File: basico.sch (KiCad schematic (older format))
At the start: 14 parts, among them P1 Power, P10 CONN_01X01, P11 CONN_01X01, P12 CONN_01X01, P13 CONN_01X01, P2 Analog, P3 Analog, P4 Digital, P5 PWM, P6 PWM, P7 Communication, P8 CONN_01X01, P9 CONN_01X01

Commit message: Empezamos a mapear cada pin
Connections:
- wire segments 172 -> 175
- no-connect marks 55 -> 83
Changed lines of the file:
@@
 Wire Wire Line
 	6950 3550 7150 3550
-NoConn ~ 3000 1750
-NoConn ~ 3000 1850
-NoConn ~ 3000 1950
 NoConn ~ 3000 2050
 NoConn ~ 3000 2150
@@
 Text Label 8900 2450 0    60   ~ 0
 A0
+NoConn ~ 8600 1550
+NoConn ~ 8900 1200
+NoConn ~ 10400 2450
+NoConn ~ 10500 4650
+NoConn ~ 8900 3800
+NoConn ~ 8900 4000
+NoConn ~ 8900 4100
+NoConn ~ 9300 5650
+NoConn ~ 9400 5650
+NoConn ~ 9500 5650
+NoConn ~ 9600 5650
+NoConn ~ 9700 5650
+NoConn ~ 9800 5650
+NoConn ~ 9900 5650
+NoConn ~ 10000 5650
+NoConn ~ 10000 4650
+NoConn ~ 10100 5650
+NoConn ~ 10300 4650
+NoConn ~ 10300 5650
+NoConn ~ 10400 5650
+NoConn ~ 10500 5650
+NoConn ~ 10400 3900
+NoConn ~ 10400 3500
+NoConn ~ 10400 1550
+NoConn ~ 10400 1650
+NoConn ~ 10400 1750
+NoConn ~ 10400 2750
+NoConn ~ 10400 2650
+NoConn ~ 10400 2550
+NoConn ~ 10400 2950
+NoConn ~ 10400 1350
+Text Label 3650 1750 0    50   ~ 0
+A0
+Wire Wire Line
+	3000 1750 3650 1750
+Wire Wire Line
+	3000 1850 3650 1850
+Text Label 3650 1850 0    50   ~ 0
+A1
+Wire Wire Line
+	3000 1950 3650 1950
+Text Label 3650 1950 0    50   ~ 0
+A2
 $EndSCHEMATC

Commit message: Mas actualizaciones de esquematico
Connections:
- net labels added: Ar_0, Ar_1, Ar_10, Ar_11, Ar_12, Ar_13, Ar_14, Ar_15, Ar_16, Ar_17, Ar_18, Ar_19, Ar_2, Ar_20, Ar_21, Ar_22, Ar_23, Ar_24, Ar_25, Ar_26, Ar_27, Ar_28, Ar_29, Ar_3, Ar_30, Ar_31, Ar_32, Ar_33, Ar_34, Ar_35, Ar_36, Ar_37, Ar_38, Ar_39, Ar_4, Ar_40, Ar_41, Ar_42, Ar_43, Ar_44, Ar_45, Ar_46, Ar_47, Ar_48, Ar_49, Ar_5, Ar_50, Ar_51, Ar_52, Ar_53, Ar_6, Ar_7, Ar_8, Ar_9, Ar_A0, Ar_A1, Ar_A10, Ar_A11, Ar_A12, Ar_A13, Ar_A14, Ar_A15, Ar_A2, Ar_A3, Ar_A4, Ar_A5, Ar_A6, Ar_A7, Ar_A8, Ar_A9, Ar_AREF, Ar_IOREF, Ar_Reset, Ar_SCL, Ar_SDA, Ar_Vin
- net labels removed: 0(Rx0), 1(Tx0), 10(**), 11(**), 12(**), 13(**), 14(Tx3), 15(Rx3), 16(Tx2), 17(Rx2), 18(Tx1), 19(Rx1), 2(**), 20(SDA), 21(SCL), 22, 23, 24, 25, 26, 27, 28, 29, 3(**), 30, 31, 32, 33, 34, 35, 36, 37, 38, 39, 4(**), 40, 41, 42, 43, 44, 45, 46, 47, 48, 49, 5(**), 50(MISO), 51(MOSI), 52(SCK), 53(SS), 6(**), 7(**), 8(**), 9(**), A0, A1, A10, A11, A12, A13, A14, A15, A2, A3, A4, A5, A6, A7, A8, A9, AREF, IOREF, Reset, SCL, SDA, Vin
- wire segments 175 -> 206
- no-connect marks 83 -> 52

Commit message: completado el esquematico
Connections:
- wire segments 206 -> 214
- no-connect marks 52 -> 44
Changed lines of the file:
@@
 L basico-rescue:GNDA #PWR017
 U 1 1 57A7AE5D
-P 5500 2000
-F 0 "#PWR017" H 5500 1750 50  0001 C CNN
-F 1 "GNDA" H 5500 1850 50  0000 C CNN
-F 2 "" H 5500 2000 50  0000 C CNN
-F 3 "" H 5500 2000 50  0000 C CNN
-	1    5500 2000
-	1    0    0    -1
-$EndComp
-Wire Wire Line
-	5750 1950 5500 1950
-Wire Wire Line
-	5500 1950 5500 2000
+P 5100 2000
+F 0 "#PWR017" H 5100 1750 50  0001 C CNN
+F 1 "GNDA" H 5100 1850 50  0000 C CNN
+F 2 "" H 5100 2000 50  0000 C CNN
+F 3 "" H 5100 2000 50  0000 C CNN
+	1    5100 2000
+	1    0    0    -1
+$EndComp
+Wire Wire Line
+	5750 1950 5100 1950
+Wire Wire Line
+	5100 1950 5100 2000
 Wire Wire Line
 	6950 1950 7000 1950
@@
 Wire Wire Line
 	6950 3550 7150 3550
-NoConn ~ 3000 2050
-NoConn ~ 3000 2150
-NoConn ~ 3000 2250
-NoConn ~ 3000 2350
-NoConn ~ 1800 2050
 NoConn ~ 1800 2350
 NoConn ~ 5750 1750
 NoConn ~ 5750 1850
-NoConn ~ 5750 2050
-NoConn ~ 5750 2150
-NoConn ~ 5750 2250
 NoConn ~ 5750 2350
 NoConn ~ 5750 2450
@@
 Wire Wire Line
 	3000 2650 3650 2650
+Text Label 3650 2850 0    50   ~ 0
+Ar_A3
+Text Label 1300 3250 0    50   ~ 0
+Ar_A4
+Text Label 3650 3050 0    50   ~ 0
+Ar_A5
+Wire Wire Line
+	1800 2050 1250 2050
+Text Label 1250 2050 0    50   ~ 0
+Ar_A6
+Wire Wire Line
+	3000 2050 3650 2050
+Text Label 3650 2050 0    50   ~ 0
+Ar_A7
+Wire Wire Line
+	3000 2150 3650 2150
+Text Label 3650 2150 0    50   ~ 0
+Ar_A8
+Wire Wire Line
+	5750 2050 5400 2050
+Wire Wire Line
+	5750 2150 5400 2150
+Wire Wire Line
+	5750 2250 5400 2250
+Text Label 3650 2650 0    50   ~ 0
+Ar_A13
+Text Label 5400 2250 0    50   ~ 0
+Ar_9
+Text Label 5400 2150 0    50   ~ 0
+Ar_10
+Text Label 5400 2050 0    50   ~ 0
+Ar_11
+Wire Wire Line
+	3000 2250 3650 2250
+Wire Wire Line
+	3000 2350 3650 2350
+Text Label 3650 2250 0    50   ~ 0
+Ar_11
+Text Label 3650 2350 0    50   ~ 0
+Ar_4
 $EndSCHEMATC

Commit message: Remove unused components. Update PCB
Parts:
- removed P10, P11, P12, P13, P8, P9: CONN_01X01, footprint:Arduino_1pin, symbol Connector_Generic:Conn_01x01
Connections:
- no-connect marks 44 -> 38
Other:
- note removed: "Holes"
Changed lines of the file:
@@
 Text Notes 8375 575  0    60   ~ 0
 Shield for Arduino Mega Rev 3
-Text Notes 10700 1000 0    60   ~ 0
-Holes
-$Comp
-L Connector_Generic:Conn_01x01 P8
-U 1 1 56D70B71
-P 10600 650
-F 0 "P8" V 10700 650 31  0000 C CNN
-F 1 "CONN_01X01" V 10700 650 50  0001 C CNN
-F 2 "footprint:Arduino_1pin" H 10600 650 50  0001 C CNN
-F 3 "" H 10600 650 50  0000 C CNN
-	1    10600 650
-	0    -1   -1   0
-$EndComp
-$Comp
-L Connector_Generic:Conn_01x01 P9
-U 1 1 56D70C9B
-P 10700 650
-F 0 "P9" V 10800 650 31  0000 C CNN
-F 1 "CONN_01X01" V 10800 650 50  0001 C CNN
-F 2 "footprint:Arduino_1pin" H 10700 650 50  0001 C CNN
-F 3 "" H 10700 650 50  0000 C CNN
-	1    10700 650
-	0    -1   -1   0
-$EndComp
-$Comp
-L Connector_Generic:Conn_01x01 P10
-U 1 1 56D70CE6
-P 10800 650
-F 0 "P10" V 10900 650 31  0000 C CNN
-F 1 "CONN_01X01" V 10900 650 50  0001 C CNN
-F 2 "footprint:Arduino_1pin" H 10800 650 50  0001 C CNN
-F 3 "" H 10800 650 50  0000 C CNN
-	1    10800 650
-	0    -1   -1   0
-$EndComp
-$Comp
-L Connector_Generic:Conn_01x01 P11
-U 1 1 56D70D2C
-P 10900 650
-F 0 "P11" V 11000 650 31  0000 C CNN
-F 1 "CONN_01X01" V 11000 650 50  0001 C CNN
-F 2 "footprint:Arduino_1pin" H 10900 650 50  0001 C CNN
-F 3 "" H 10900 650 50  0000 C CNN
-	1    10900 650
-	0    -1   -1   0
-$EndComp
-$Comp
-L Connector_Generic:Conn_01x01 P12
-U 1 1 56D711A2
-P 11000 650
-F 0 "P12" V 11100 650 31  0000 C CNN
-F 1 "CONN_01X01" V 11100 650 50  0001 C CNN
-F 2 "footprint:Arduino_1pin" H 11000 650 50  0001 C CNN
-F 3 "" H 11000 650 50  0000 C CNN
-	1    11000 650
-	0    -1   -1   0
-$EndComp
-$Comp
-L Connector_Generic:Conn_01x01 P13
-U 1 1 56D711F0
-P 11100 650
-F 0 "P13" V 11200 650 31  0000 C CNN
-F 1 "CONN_01X01" V 11200 650 50  0001 C CNN
-F 2 "footprint:Arduino_1pin" H 11100 650 50  0001 C CNN
-F 3 "" H 11100 650 50  0000 C CNN
-	1    11100 650
-	0    -1   -1   0
-$EndComp
-NoConn ~ 10600 850
-NoConn ~ 10700 850
-NoConn ~ 10800 850
-NoConn ~ 10900 850
-NoConn ~ 11000 850
-NoConn ~ 11100 850
 Text Notes 9650 1350 0    60   ~ 0
 1
@@
 	9350 1450 9250 1450
 Wire Notes Line
-	10450 1000 10450 500
-Wire Notes Line
-	11200 1000 10450 1000
-Wire Notes Line
 	9850 650  9850 475

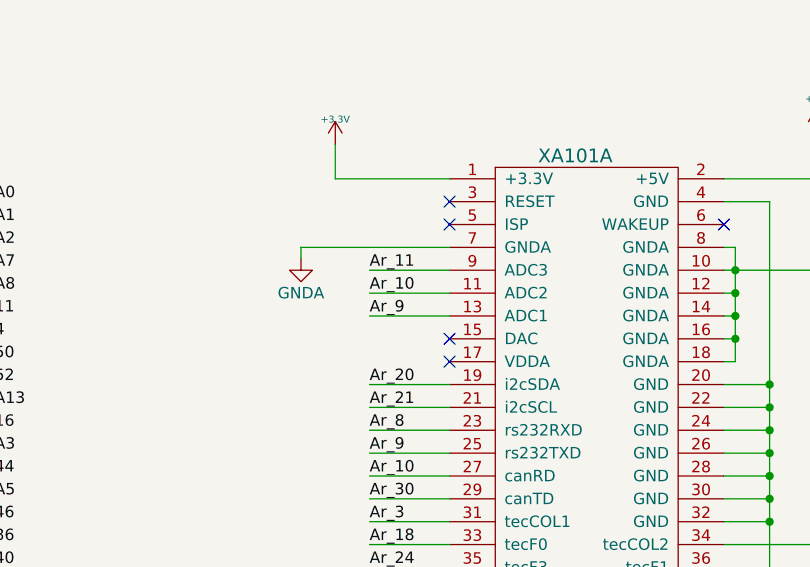
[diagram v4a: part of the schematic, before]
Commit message: Fix wrong mapping for analog channels
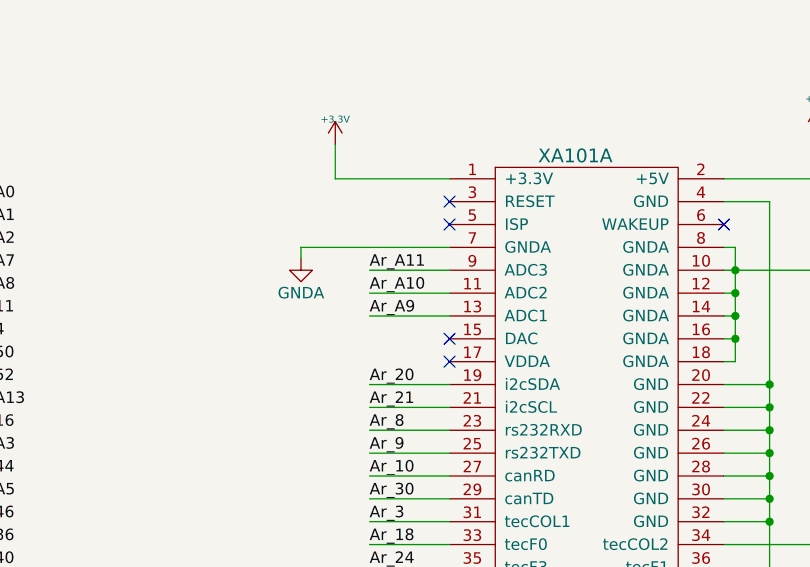
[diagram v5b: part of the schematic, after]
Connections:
- net Ar_10: no longer XA101.11 (ADC2)
- net Ar_11: no longer XA101.9 (ADC3)
- net Ar_9: no longer XA101.13 (ADC1)
- net Ar_A10: now also XA101.11 (ADC2)
- net Ar_A11: now also XA101.9 (ADC3)
- net Ar_A9: now also XA101.13 (ADC1)
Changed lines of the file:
@@
 Ar_A13
 Text Label 5400 2250 0    50   ~ 0
-Ar_9
+Ar_A9
 Text Label 5400 2150 0    50   ~ 0
-Ar_10
+Ar_A10
 Text Label 5400 2050 0    50   ~ 0
-Ar_11
+Ar_A11
 Wire Wire Line
 	3000 2250 3650 2250

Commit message: All routes done
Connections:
- net +3.3VP: no longer XA101.1 (+3.3V)
- net +5V: no longer P4.35 (Pin_35), P4.36 (Pin_36), XA101.2 (+5V)
- net GND: no longer P4.1 (Pin_1), P4.2 (Pin_2), XA101.20 (GND), XA101.22 (GND), XA101.24 (GND), XA101.26 (GND), XA101.28 (GND), XA101.30 (GND), XA101.32 (GND), XA101.38 (GND), XA101.4 (GND), XA101.40 (GND), XA101.51 (GND), XA101.53 (GND), XA101.57 (GND), XA101.59 (GND), XA101.65 (GND), XA101.67 (GND), XA101.77 (GND), XA101.79 (GND)
- no-connect marks 38 -> 62
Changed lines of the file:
@@
-$EndComp
-$Comp
-L basico-rescue:+3.3V #PWR01
-U 1 1 560EB699
-P 5250 1500
-F 0 "#PWR01" H 5250 1460 30  0001 C CNN
-F 1 "+3.3V" H 5250 1610 30  0000 C CNN
-F 2 "" H 5250 1500 60  0000 C CNN
-F 3 "" H 5250 1500 60  0000 C CNN
-	1    5250 1500
-	1    0    0    -1
-$EndComp
-$Comp
-L basico-rescue:+5V #PWR02
-U 1 1 560EB7BE
-P 7350 1450
-F 0 "#PWR02" H 7350 1540 20  0001 C CNN
-F 1 "+5V" H 7350 1600 30  0000 C CNN
-F 2 "" H 7350 1450 60  0000 C CNN
-F 3 "" H 7350 1450 60  0000 C CNN
-	1    7350 1450
-	1    0    0    -1
 $EndComp
 $Comp
 L basico-rescue:PWR_FLAG #FLG04
 U 1 1 560EDE73
-P 1300 3600
-F 0 "#FLG04" H 1300 3695 30  0001 C CNN
-F 1 "PWR_FLAG" H 1300 3780 30  0000 C CNN
-F 2 "" H 1300 3600 60  0000 C CNN
-F 3 "" H 1300 3600 60  0000 C CNN
-	1    1300 3600
+P 700 1900
+F 0 "#FLG04" H 700 1995 30  0001 C CNN
+F 1 "PWR_FLAG" H 700 2080 30  0000 C CNN
+F 2 "" H 700 1900 60  0000 C CNN
+F 3 "" H 700 1900 60  0000 C CNN
+	1    700  1900
 	-1   0    0    1
 $EndComp
@@
 	1    0    0    -1
 $EndComp
-$Comp
-L basico-rescue:GND #PWR06
-U 1 1 57A7A207
-P 7150 3750
-F 0 "#PWR06" H 7150 3750 30  0001 C CNN
-F 1 "GND" H 7150 3680 30  0001 C CNN
-F 2 "" H 7150 3750 60  0000 C CNN
-F 3 "" H 7150 3750 60  0000 C CNN
-	1    7150 3750
-	1    0    0    -1
-$EndComp
-Wire Wire Line
-	7150 1750 7150 2550
-Wire Wire Line
-	7150 3450 6950 3450
-Connection ~ 7150 3550
-Wire Wire Line
-	7150 3150 6950 3150
-Connection ~ 7150 3450
-Wire Wire Line
-	7150 3050 6950 3050
-Connection ~ 7150 3150
-Wire Wire Line
-	7150 2950 6950 2950
-Connection ~ 7150 3050
-Wire Wire Line
-	7150 2850 6950 2850
-Connection ~ 7150 2950
-Wire Wire Line
-	7150 2550 6950 2550
-Connection ~ 7150 2850
-Wire Wire Line
-	6950 2650 7150 2650
-Connection ~ 7150 2650
-Wire Wire Line
-	6950 2750 7150 2750
-Connection ~ 7150 2750
-Wire Wire Line
-	6950 1750 7150 1750
-Connection ~ 7150 2550
 Wire Wire Line
 	1600 1750 1600 1850
 Wire Wire Line
-	1600 3450 1800 3450
-Connection ~ 1600 3550
-Wire Wire Line
-	1600 2950 1800 2950
-Connection ~ 1600 3450
-Wire Wire Line
-	1600 2850 1800 2850
-Connection ~ 1600 2950
-Wire Wire Line
-	1600 2550 1800 2550
-Connection ~ 1600 2850
-Wire Wire Line
-	1600 2450 1800 2450
-Connection ~ 1600 2550
-Wire Wire Line
-	1600 2250 1800 2250
-Connection ~ 1600 2450
-Wire Wire Line
-	1600 2150 1800 2150
-Connection ~ 1600 2250
-Wire Wire Line
 	1600 1950 1800 1950
-Connection ~ 1600 2150
 Wire Wire Line
 	1600 1850 1800 1850
-Connection ~ 1600 1950
 Wire Wire Line
 	1600 1750 1800 1750
@@
 L basico-rescue:GNDD #PWR012
 U 1 1 57A7AB5F
-P 1600 3700
-F 0 "#PWR012" H 1600 3450 50  0001 C CNN
-F 1 "GNDD" H 1600 3550 50  0000 C CNN
-F 2 "" H 1600 3700 50  0000 C CNN
-F 3 "" H 1600 3700 50  0000 C CNN
-	1    1600 3700
+P 1000 2000
+F 0 "#PWR012" H 1000 1750 50  0001 C CNN
+F 1 "GNDD" H 1000 1850 50  0000 C CNN
+F 2 "" H 1000 2000 50  0000 C CNN
+F 3 "" H 1000 2000 50  0000 C CNN
+	1    1000 2000
 	1    0    0    -1
 $EndComp
@@
 	1    0    0    -1
 $EndComp
-$Comp
-L basico-rescue:GNDA #PWR017
-U 1 1 57A7AE5D
-P 5100 2000
-F 0 "#PWR017" H 5100 1750 50  0001 C CNN
-F 1 "GNDA" H 5100 1850 50  0000 C CNN
-F 2 "" H 5100 2000 50  0000 C CNN
-F 3 "" H 5100 2000 50  0000 C CNN
-	1    5100 2000
-	1    0    0    -1
-$EndComp
-Wire Wire Line
-	5750 1950 5100 1950
-Wire Wire Line
-	5100 1950 5100 2000
 Wire Wire Line
 	6950 1950 7000 1950
@@
 Wire Wire Line
 	3450 1650 3450 1400
-Wire Wire Line
-	5250 1650 5250 1500
-Wire Wire Line
-	6950 1650 7350 1650
-Wire Wire Line
-	7350 1650 7350 1450
-Wire Wire Line
-	5250 1650 5750 1650
-Wire Wire Line
-	6950 3550 7150 3550
 NoConn ~ 1800 2350
 NoConn ~ 5750 1750
@@
 NoConn ~ 6950 1850
 Wire Wire Line
-	7150 3550 7150 3750
-Wire Wire Line
-	7150 3450 7150 3550
-Wire Wire Line
-	7150 3150 7150 3450
-Wire Wire Line
-	7150 3050 7150 3150
-Wire Wire Line
-	7150 2950 7150 3050
-Wire Wire Line
-	7150 2850 7150 2950
-Wire Wire Line
-	7150 2650 7150 2750
-Wire Wire Line
-	7150 2750 7150 2850
-Wire Wire Line
-	7150 2550 7150 2650
-Wire Wire Line
-	1600 3550 1600 3700
-Wire Wire Line
-	1600 3550 1800 3550
-Wire Wire Line
-	1600 3450 1600 3550
-Wire Wire Line
-	1600 2950 1600 3450
-Wire Wire Line
-	1600 2850 1600 2950
-Wire Wire Line
-	1600 2550 1600 2850
-Wire Wire Line
-	1600 2450 1600 2550
-Wire Wire Line
-	1600 2250 1600 2450
-Wire Wire Line
-	1600 2150 1600 2250
-Wire Wire Line
-	1600 1950 1600 2150
+	1000 1850 1000 2000
+Wire Wire Line
+	1000 1850 1600 1850
 Wire Wire Line
 	1600 1850 1600 1950
@@
 Wire Wire Line
 	10250 1450 10150 1450
-$Comp
-L power:GND #PWR0103
-U 1 1 56D758F6
-P 8650 5750
-F 0 "#PWR0103" H 8650 5500 50  0001 C CNN
-F 1 "GND" H 8650 5600 50  0000 C CNN
-F 2 "" H 8650 5750 50  0000 C CNN
-F 3 "" H 8650 5750 50  0000 C CNN
-	1    8650 5750
-	1    0    0    -1
-$EndComp
 Wire Notes Line
 	11200 6050 8350 6050
@@
 Text Notes 7850 -250 0    79   Italic 16
 Este diseño puede copiarse para iniciar un poncho simple. \n1) Copiar toda la carpeta "Basico" , renombrando \n   la misma al nombre del poncho.\n2) Renombrar los archivos "basico.xxx" manteniendo \n    las extensiones pero cambiando a un nombre \n    descriptivo del poncho. Evitar acentos, espacios y \n    caracteres ascii esxtendidos.
-Wire Wire Line
-	8650 5350 8650 5750
-Wire Wire Line
-	8650 4850 8650 5350
-Wire Wire Line
-	10750 4850 10750 5350
-Wire Wire Line
-	10750 4550 10750 4850
-Connection ~ 10750 4850
-$Comp
-L power:+5V #PWR0104
-U 1 1 56D75AB8
-P 10750 4550
-F 0 "#PWR0104" H 10750 4400 50  0001 C CNN
-F 1 "+5V" H 10750 4690 50  0000 C CNN
-F 2 "" H 10750 4550 50  0000 C CNN
-F 3 "" H 10750 4550 50  0000 C CNN
-	1    10750 4550
-	1    0    0    -1
-$EndComp
-Wire Wire Line
-	10750 4850 10600 4850
-Wire Wire Line
-	10750 5350 10600 5350
-Connection ~ 8650 5350
-Wire Wire Line
-	8900 5350 8650 5350
-Wire Wire Line
-	8900 4850 8650 4850
 Wire Wire Line
 	9000 5350 9000 5750
@@
 	1800 3250 1300 3250
 Wire Wire Line
-	1300 3600 1300 3550
-Wire Wire Line
-	1300 3550 1600 3550
+	700  1900 700  1850
+Wire Wire Line
+	700  1850 1000 1850
 Wire Wire Line
 	1800 3350 1300 3350
@@
 Text Label 3650 2350 0    50   ~ 0
 Ar_4
+NoConn ~ 6950 1650
+NoConn ~ 5750 1650
+Wire Wire Line
+	5100 1950 5100 2000
+Wire Wire Line
+	5750 1950 5100 1950
+$Comp
+L basico-rescue:GNDA #PWR017
+U 1 1 57A7AE5D
+P 5100 2000
+F 0 "#PWR017" H 5100 1750 50  0001 C CNN
+F 1 "GNDA" H 5100 1850 50  0000 C CNN
+F 2 "" H 5100 2000 50  0000 C CNN
+F 3 "" H 5100 2000 50  0000 C CNN
+	1    5100 2000
+	1    0    0    -1
+$EndComp
+NoConn ~ 6950 3450
+NoConn ~ 6950 3550
+NoConn ~ 6950 2550
+NoConn ~ 6950 2650
+NoConn ~ 6950 2750
+NoConn ~ 6950 2850
+NoConn ~ 6950 2950
+NoConn ~ 6950 3050
+NoConn ~ 6950 3150
+NoConn ~ 6950 1750
+Connection ~ 1000 1850
+NoConn ~ 1800 2150
+NoConn ~ 1800 2250
+NoConn ~ 1800 2550
+NoConn ~ 1800 2450
+NoConn ~ 1800 2950
+NoConn ~ 1800 2850
+NoConn ~ 1800 3450
+NoConn ~ 1800 3550
+NoConn ~ 10600 4850
+NoConn ~ 10600 5350
+NoConn ~ 8900 5350
+NoConn ~ 8900 4850
 $EndSCHEMATC

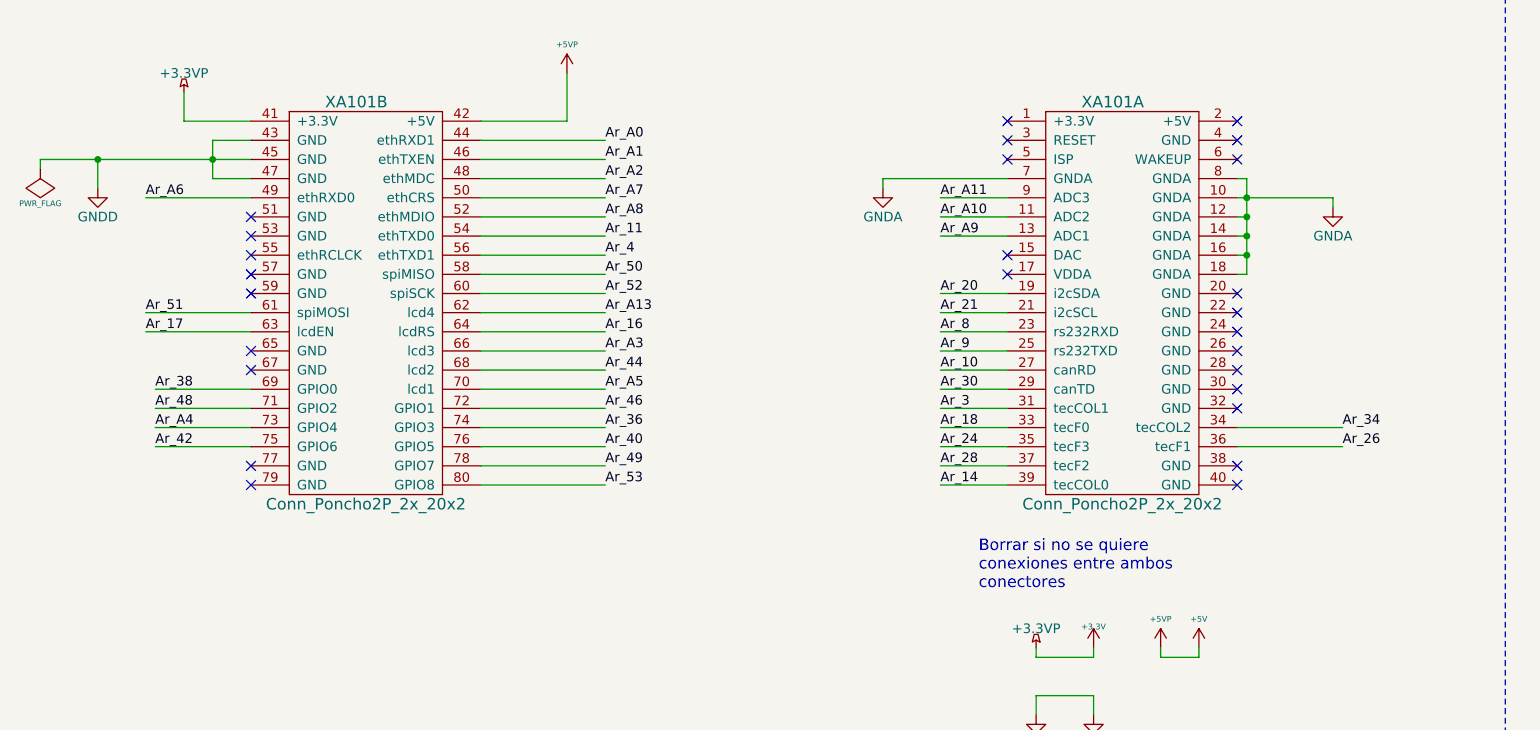
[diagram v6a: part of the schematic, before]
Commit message: Fix unconnected pin
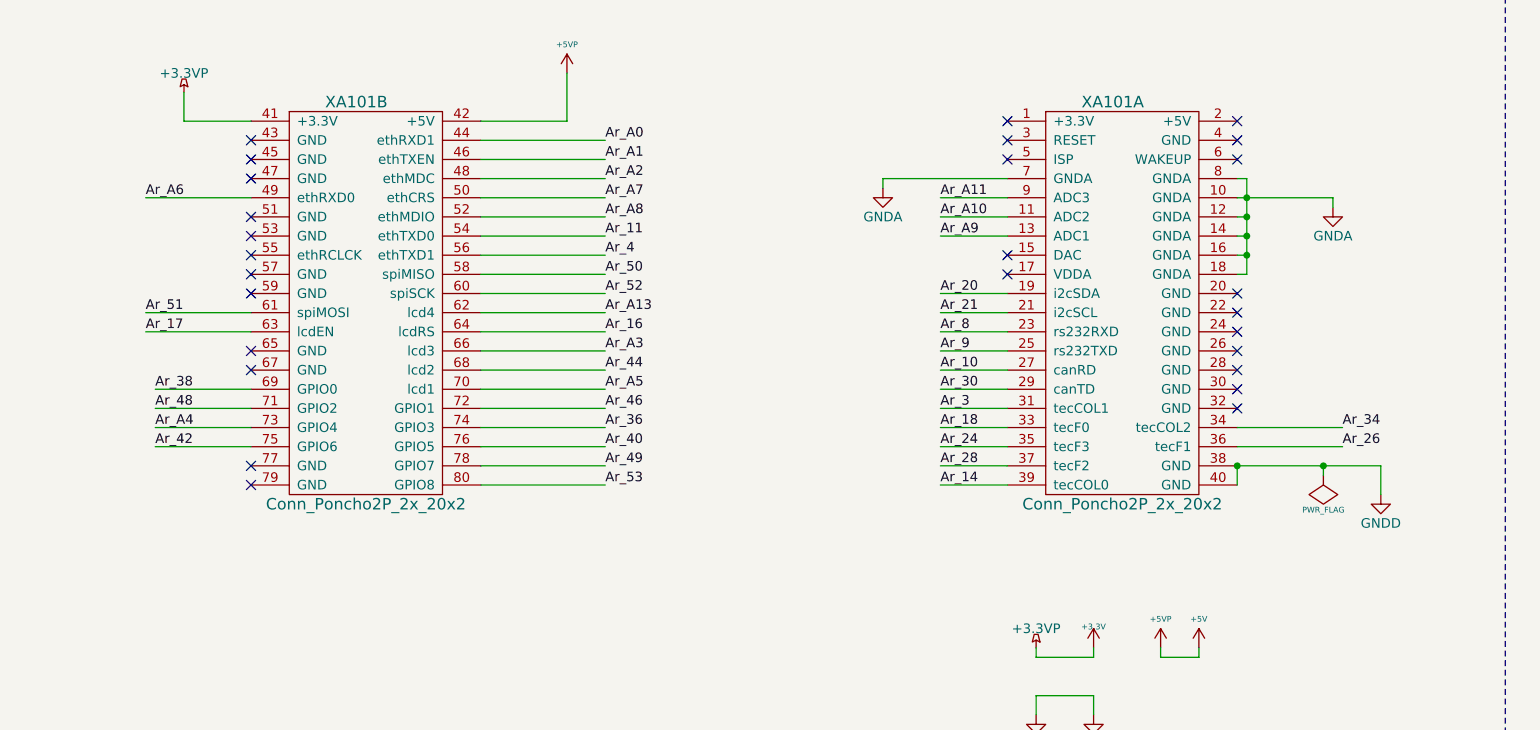
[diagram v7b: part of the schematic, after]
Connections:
- net GND: now also XA101.38 (GND), XA101.40 (GND); no longer XA101.43 (GND), XA101.45 (GND), XA101.47 (GND)
- no-connect marks 62 -> 63
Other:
- note removed: "Borrar si no se quiere \nconexiones entre ambos \nconectores"
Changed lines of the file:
@@
 L basico-rescue:PWR_FLAG #FLG04
 U 1 1 560EDE73
-P 700 1900
-F 0 "#FLG04" H 700 1995 30  0001 C CNN
-F 1 "PWR_FLAG" H 700 2080 30  0000 C CNN
-F 2 "" H 700 1900 60  0000 C CNN
-F 3 "" H 700 1900 60  0000 C CNN
-	1    700  1900
+P 7400 3500
+F 0 "#FLG04" H 7400 3595 30  0001 C CNN
+F 1 "PWR_FLAG" H 7400 3680 30  0000 C CNN
+F 2 "" H 7400 3500 60  0000 C CNN
+F 3 "" H 7400 3500 60  0000 C CNN
+	1    7400 3500
 	-1   0    0    1
 $EndComp
@@
 	1    0    0    -1
 $EndComp
-Wire Wire Line
-	1600 1750 1600 1850
-Wire Wire Line
-	1600 1950 1800 1950
-Wire Wire Line
-	1600 1850 1800 1850
-Wire Wire Line
-	1600 1750 1800 1750
-Connection ~ 1600 1850
 $Comp
 L basico-rescue:+3.3VP #PWR07
@@
 Wire Wire Line
 	6750 4450 6750 4400
-Text Notes 5600 4100 0    60   ~ 0
-Borrar si no se quiere \nconexiones entre ambos \nconectores
 $Comp
 L basico-rescue:GNDD #PWR012
 U 1 1 57A7AB5F
-P 1000 2000
-F 0 "#PWR012" H 1000 1750 50  0001 C CNN
-F 1 "GNDD" H 1000 1850 50  0000 C CNN
-F 2 "" H 1000 2000 50  0000 C CNN
-F 3 "" H 1000 2000 50  0000 C CNN
-	1    1000 2000
+P 7700 3600
+F 0 "#PWR012" H 7700 3350 50  0001 C CNN
+F 1 "GNDD" H 7700 3450 50  0000 C CNN
+F 2 "" H 7700 3600 50  0000 C CNN
+F 3 "" H 7700 3600 50  0000 C CNN
+	1    7700 3600
 	1    0    0    -1
 $EndComp
@@
 NoConn ~ 6950 1850
 Wire Wire Line
-	1000 1850 1000 2000
-Wire Wire Line
-	1000 1850 1600 1850
-Wire Wire Line
-	1600 1850 1600 1950
+	7700 3450 7700 3600
+Wire Wire Line
+	7700 3450 7400 3450
 Wire Wire Line
 	7000 2350 7000 2450
@@
 	1800 3250 1300 3250
 Wire Wire Line
-	700  1900 700  1850
-Wire Wire Line
-	700  1850 1000 1850
+	7400 3500 7400 3450
 Wire Wire Line
 	1800 3350 1300 3350
@@
 	1    0    0    -1
 $EndComp
-NoConn ~ 6950 3450
-NoConn ~ 6950 3550
 NoConn ~ 6950 2550
 NoConn ~ 6950 2650
@@
 NoConn ~ 6950 3150
 NoConn ~ 6950 1750
-Connection ~ 1000 1850
 NoConn ~ 1800 2150
 NoConn ~ 1800 2250
@@
 NoConn ~ 8900 5350
 NoConn ~ 8900 4850
+Connection ~ 7400 3450
+Wire Wire Line
+	7400 3450 6950 3450
+Wire Wire Line
+	6950 3550 6950 3450
+Connection ~ 6950 3450
+NoConn ~ 1800 1750
+NoConn ~ 1800 1850
+NoConn ~ 1800 1950
 $EndSCHEMATC
